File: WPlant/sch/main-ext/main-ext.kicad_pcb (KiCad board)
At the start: 2 copper layers, 156 parts, among them J1 PROG/JTAG, J10 Ext, J11 HSensor, J12 HSensor, J13 HSensor, J14 HSensor, J15 HSensor, J16 HSensor, J17 HSensor, J18 WaterLevel, J2 Battery, J3 Balance, J4 DE9_Receptacle, J6 Conn_01x08_Pin, J9 Leak, M1 Motor_DC, Q1 FDS9926A, Q2 FDS9926A, Q3 FDS9926A, Q4 FDS9926A, Q6 Si2301, Q7 BC817, SW1 SW_Push, SW2 SW_Push, SW3 SW_Push, U1 SIWG917Y121MGABAR, U10 SP485EEN-L/TR, U11 TXU0102QDCURQ1, U12 CD74HCT4051M96, U13 CD74HCT4051M96, U14 SN74LVC1G14DBV, U2 AP64352SP-13, U3 AP64352SP-13, U4 AP64352SP-13, U6 AP2204R-5.0, U7 74HC594, U9 INA180A2, X1 SIT1552AI-JE-DCC-32.768D

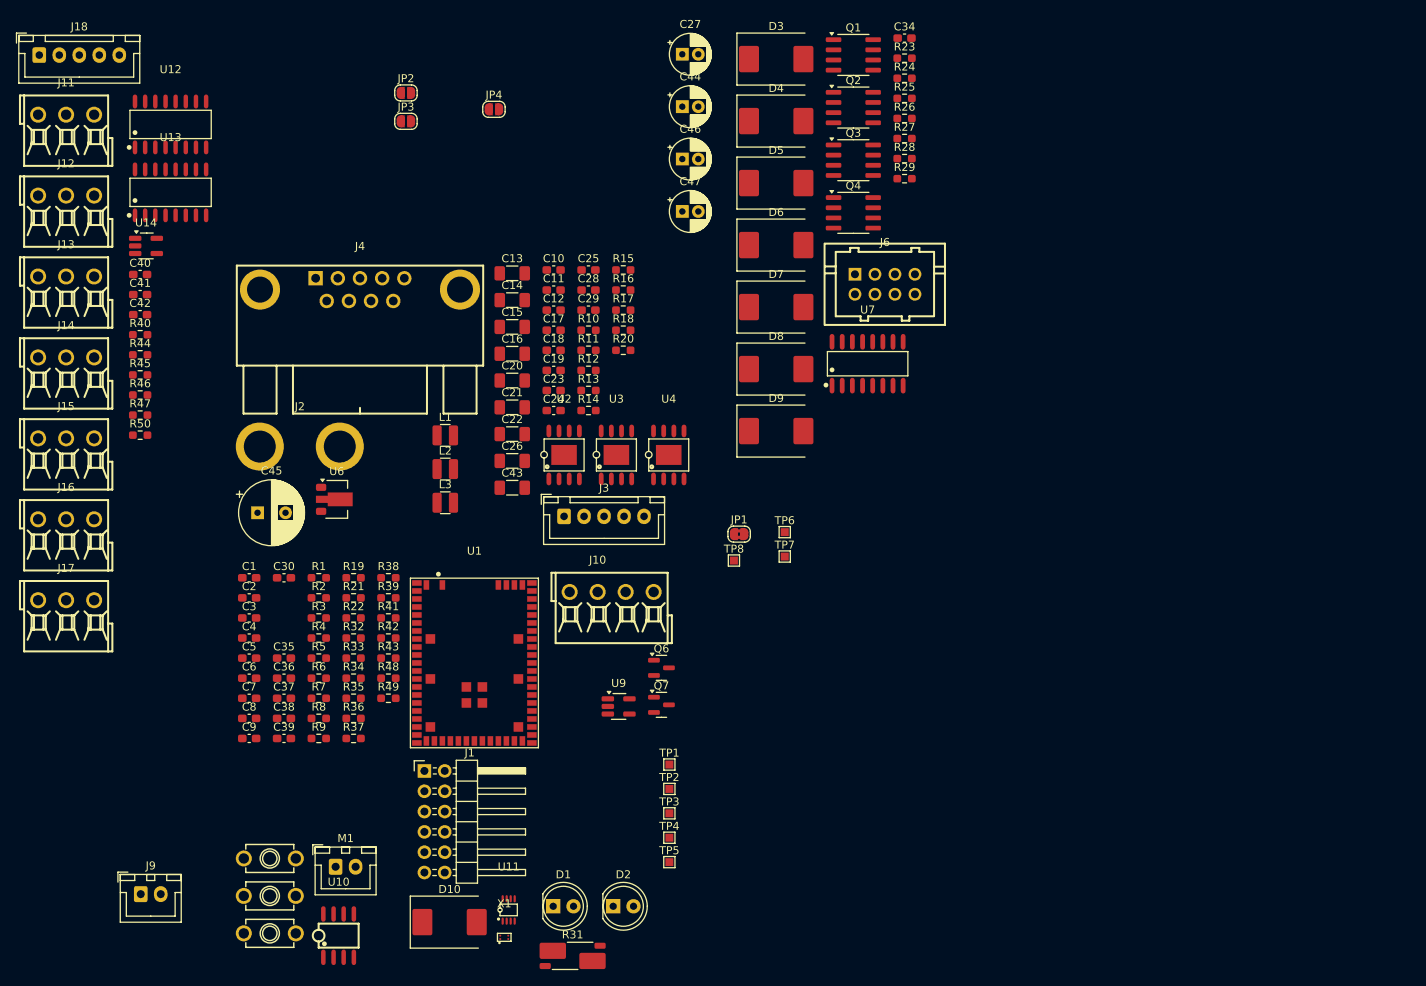
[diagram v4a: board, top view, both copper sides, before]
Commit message: Route of MainInt PCB done
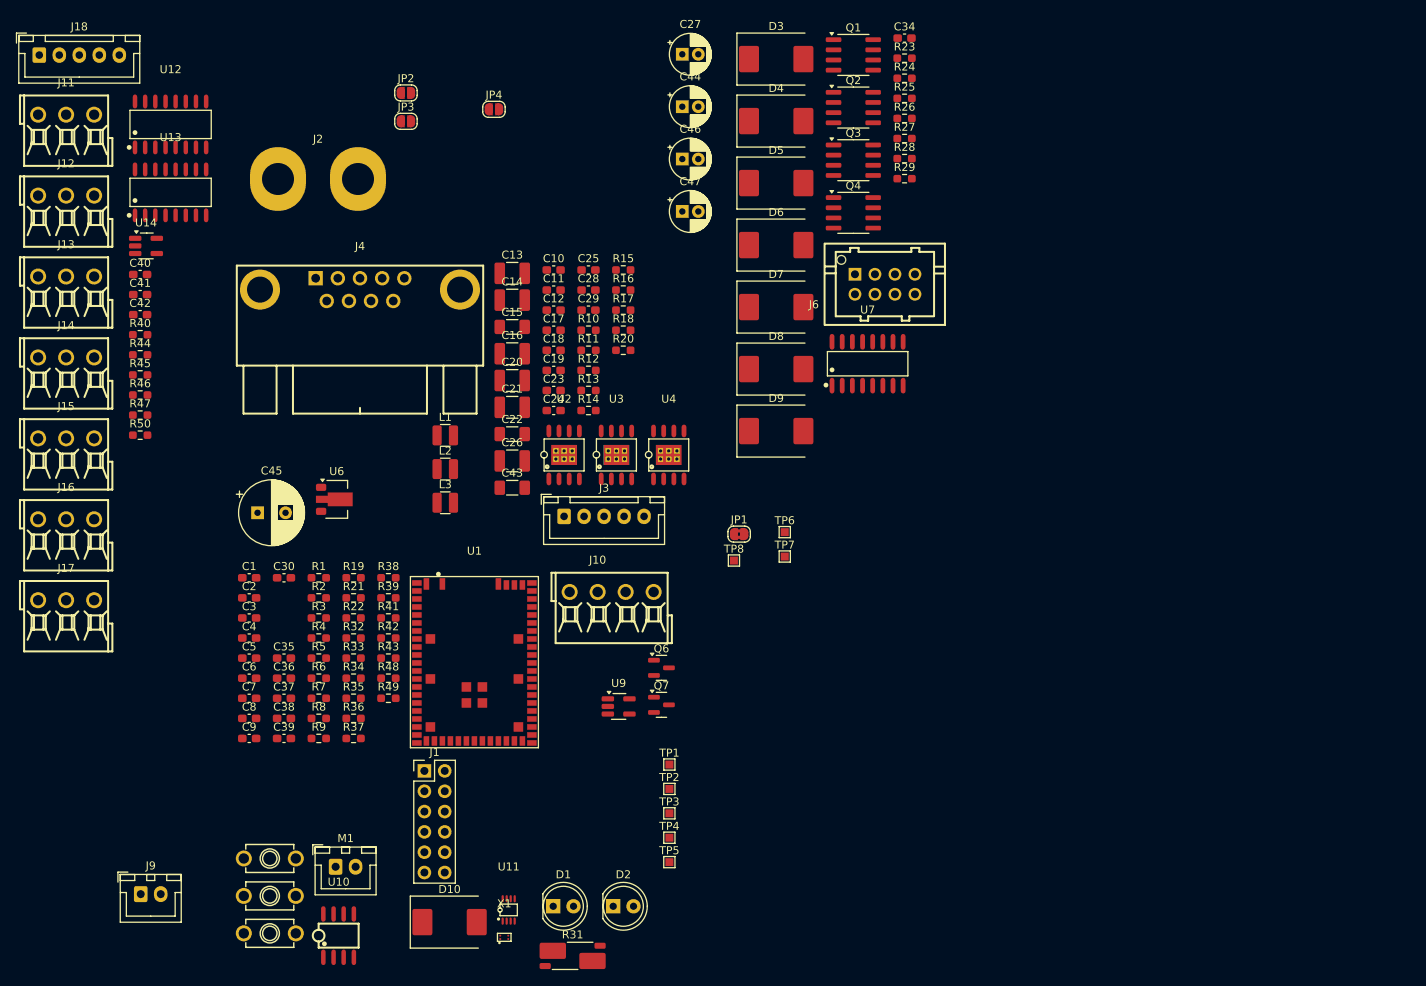
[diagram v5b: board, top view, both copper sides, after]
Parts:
- C13, C14, C16, C20, C21, C26: footprint Capacitor_SMD:C_1206_3216Metric_Pad1.33x1.80mm_HandSolder -> Capacitor_SMD:C_1210_3225Metric_Pad1.33x2.70mm_HandSolder
- J1: footprint locals:PinHeader_2x06_P2.54mm_HorizontalAB -> locals:PinHeader_2x06_P2.54mm_VerticalAB
- J6: footprint easyeda2kicad:CONN-TH_8P-P2.50_XAD-8A -> locals:CONN-TH_8P-P2.50_XAD-8AS
- U1: footprint easyeda2kicad:COMM-SMD_SIWG917Y110LGNBA -> locals:COMM-SMD_SIWG917Y110LGNBA
- U2, U3, U4: footprint easyeda2kicad:SO-8_L4.9-W3.9-P1.27-LS6.0-BL-EP -> locals:SO-8_L4.9-W3.9-P1.27-LS6.0-BL-EP
- moved J2 33.5 mm to (93.6, 57.2)

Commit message: Route of MainExt PCB done
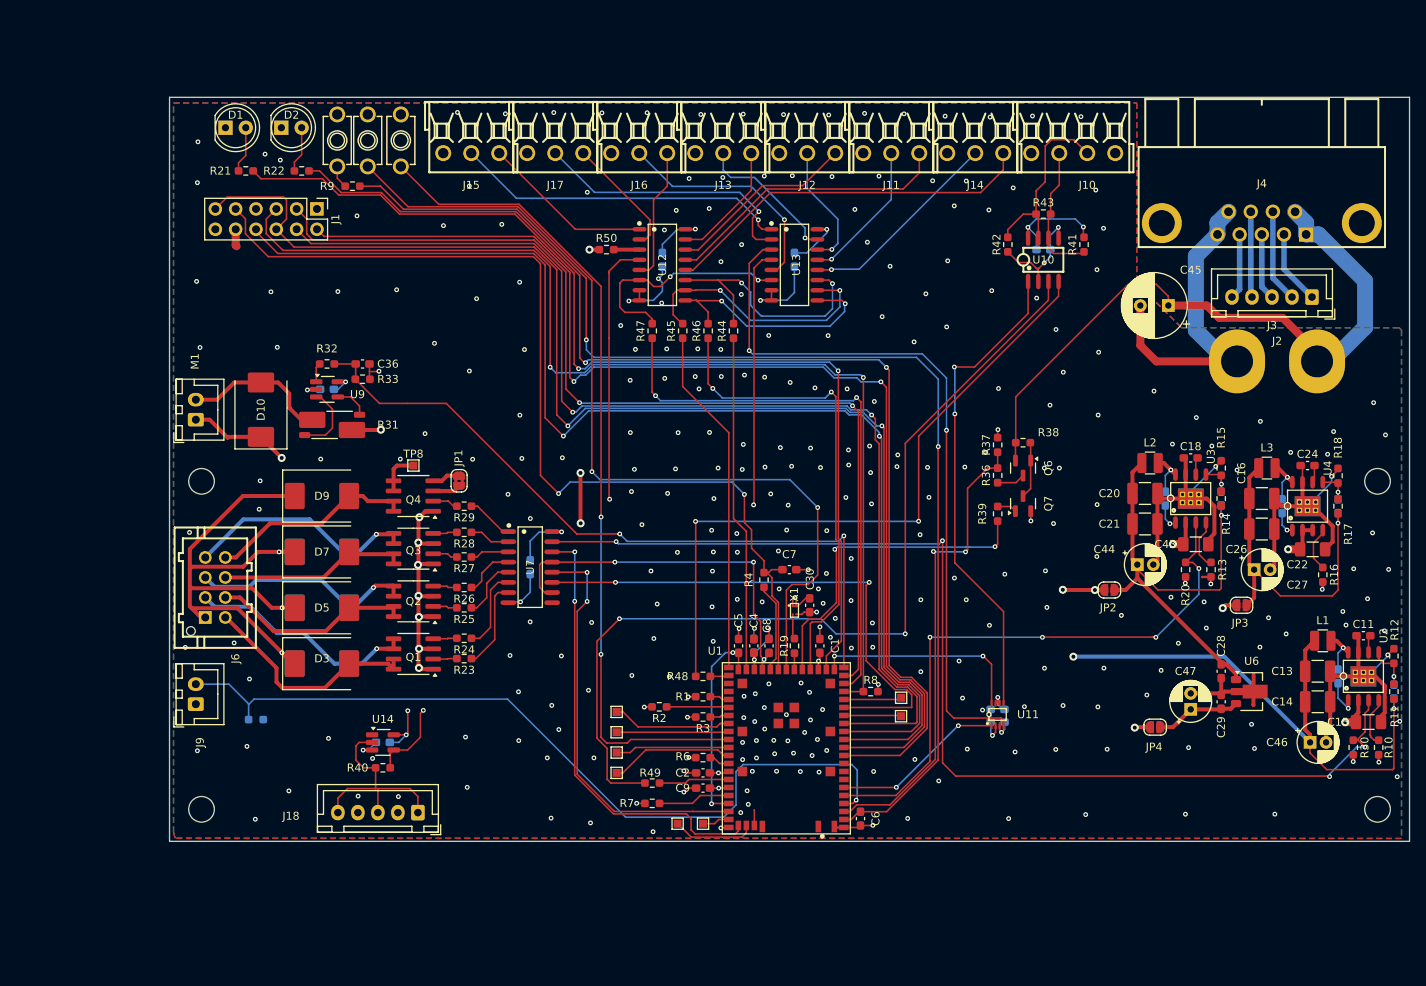
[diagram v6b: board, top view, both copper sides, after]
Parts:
- removed R34: 510, Resistor_SMD:R_0603_1608Metric_Pad0.98x0.95mm_HandSolder
- added H1: MountingHole, MountingHole:MountingHole_3.2mm_M3, F.Cu at (84.0, 95.0)
- added H2: MountingHole, MountingHole:MountingHole_3.2mm_M3, F.Cu at (231.0, 95.0)
- added H3: MountingHole, MountingHole:MountingHole_3.2mm_M3, F.Cu at (231.0, 136.0)
- added H4: MountingHole, MountingHole:MountingHole_3.2mm_M3, F.Cu at (84.0, 136.0)
- added R30: 200K, Resistor_SMD:R_0603_1608Metric_Pad0.98x0.95mm_HandSolder, F.Cu at (228.0, 128.3)
- added TP9: TestPoint, TestPoint:TestPoint_Pad_1.0x1.0mm, F.Cu at (146.7, 137.8)
- C10, C12, C17, C19, C23, C25, C3, C34, C35, C37, C38, C39, C40, C41, C42, D4, D6, D8, R35, R5: moved to B.Cu
- moved U10 122.1 mm to (189.2, 67.3)
- moved J2 122.0 mm to (213.4, 80.0)
- moved JP3 120.7 mm to (214.0, 110.5), turned to 180 degrees
- moved C15 117.9 mm to (229.9, 125.1), turned to 180 degrees
- moved U6 116.9 mm to (215.3, 121.3)
- moved C45 116.8 mm to (204.9, 73.0), turned to 180 degrees
- moved J14 116.5 mm to (180.7, 54.0), turned to 180 degrees
- moved C12 115.3 mm to (233.0, 121.3), turned to -90 degrees
- moved JP4 113.1 mm to (203.2, 125.7), turned to 180 degrees
- moved J4 113.0 mm to (216.5, 62.7), turned to 180 degrees
- moved L1 112.7 mm to (224.2, 114.9), turned to 180 degrees
- moved C14 112.5 mm to (223.5, 122.6), turned to 180 degrees
- moved C13 112.3 mm to (223.5, 118.7), turned to 180 degrees
- moved R10 111.7 mm to (231.1, 128.3), turned to -90 degrees
- moved C10 110.4 mm to (226.1, 119.4), turned to 90 degrees
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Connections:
- R23 pad 1: Net-(U7-QA) -> Net-(U7-QH)
- R24 pad 1: Net-(U7-QB) -> Net-(U7-QG)
- R25 pad 1: Net-(U7-QC) -> Net-(U7-QF)
- R26 pad 1: Net-(U7-QD) -> Net-(U7-QE)
- R27 pad 1: Net-(U7-QE) -> Net-(U7-QD)
- R28 pad 1: Net-(U7-QF) -> Net-(U7-QC)
- R29 pad 1: Net-(U7-QG) -> Net-(U7-QB)
- TP5 pad 1: Net-(U1-ULP_GPIO_1) -> Net-(U1-GPIO_15)
- U1 pad 28: Net-(U1-ULP_GPIO_1) -> /AccSence
- U1 pad 56: /Valves/MOSI -> Net-(U1-GPIO_12)
- U1 pad 58: Net-(U1-GPIO_11) -> /Valves/MOSI
- U1 pad 59: /AccSence -> Net-(U1-GPIO_15)
- U7 pad 15: Net-(U7-QA) -> /Power/EN12
- U7 pad 7: /Power/EN12 -> Net-(U7-QH)
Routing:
- net GND: track 0.00 -> 277.7 mm, vias 0 -> 325
- net +9V: track 0.00 -> 265.5 mm, vias 0 -> 5
- net +3.3V: track 0.00 -> 211.8 mm, vias 0 -> 16
- net +5V: track 0.00 -> 211.5 mm, vias 0 -> 8
- net /Power/12V: track 0.00 -> 209.2 mm, vias 0 -> 3
- net VBUS: track 0.00 -> 170.8 mm, vias 0 -> 3
- net JTAG-TDO: track 0.00 -> 163.0 mm, vias 0 -> 2
- net JTAG-TCK: track 0.00 -> 151.5 mm, vias 0 -> 2
- net Net-(U1-UULP_VBAT_GPIO_0): track 0.00 -> 150.0 mm, vias 0 -> 2
- net Net-(U1-GPIO_55): track 0.00 -> 148.5 mm, vias 0 -> 2
- net JTAG-TMS: track 0.00 -> 144.9 mm, vias 0 -> 2
- net JTAG-TDI: track 0.00 -> 142.4 mm, vias 0 -> 2
- net /Power/EN12: track 0.00 -> 139.9 mm, vias 0 -> 4
- net PROG-RX: track 0.00 -> 135.9 mm, vias 0 -> 2
- net Net-(U1-GPIO_52): track 0.00 -> 129.1 mm, vias 0 -> 2
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- added copper zone on In1.Cu, net +3.3V
- added copper zone on B.Cu, net GND
- added copper zone on F.Cu, net GND
- added copper zone on In1.Cu, net GND
- added copper zone on In2.Cu, net GND
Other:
- board outline added: 155 x 93 mm
- copper layers 2 -> 4

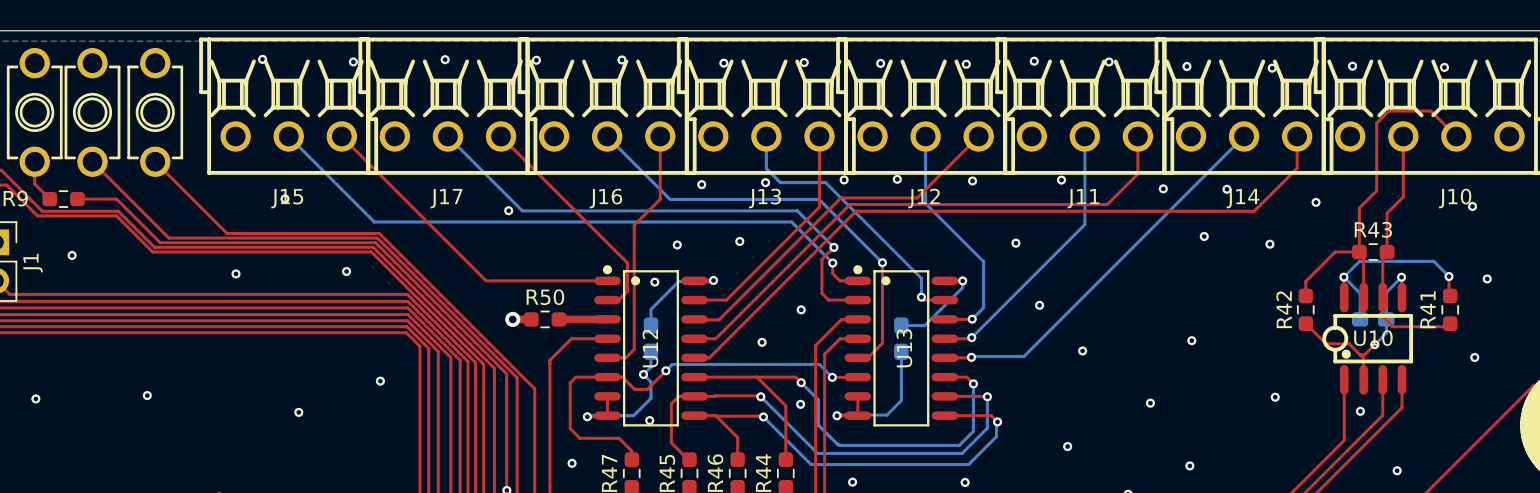
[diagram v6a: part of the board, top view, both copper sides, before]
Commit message: Route of WP project done
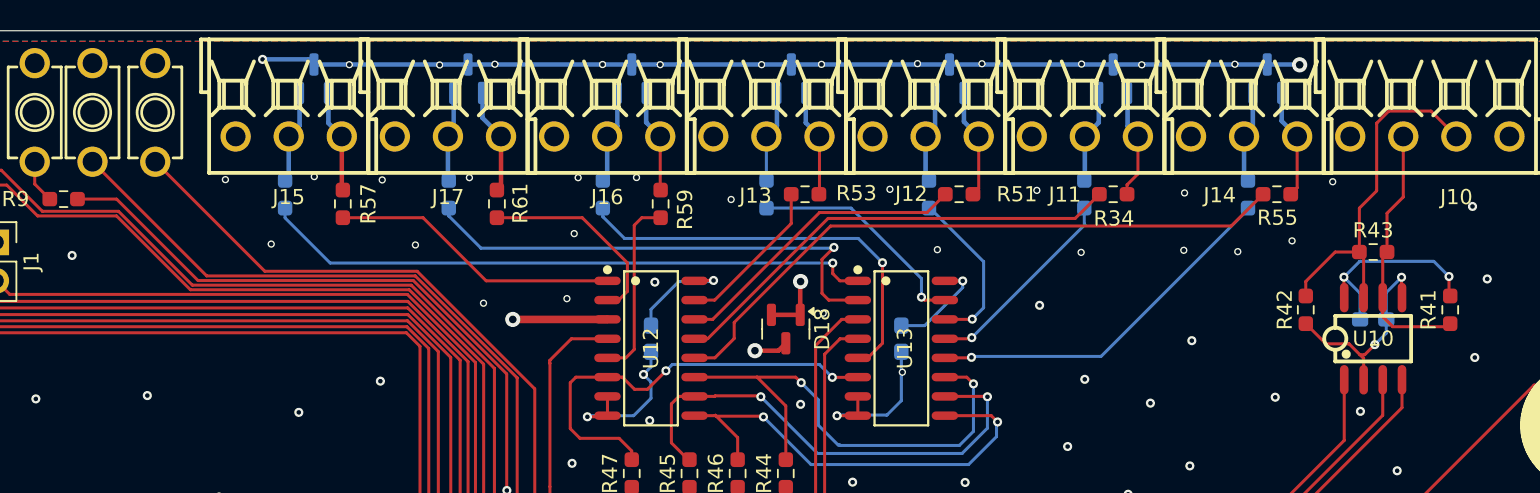
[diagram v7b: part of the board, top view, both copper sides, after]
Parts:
- added D11: MMBZ5V6, Package_TO_SOT_SMD:SOT-23, B.Cu at (172.1, 50.2)
- added D12: MMBZ5V6, Package_TO_SOT_SMD:SOT-23, B.Cu at (161.3, 50.2)
- added D13: MMBZ5V6, Package_TO_SOT_SMD:SOT-23, B.Cu at (150.9, 50.2)
- added D14: MMBZ5V6, Package_TO_SOT_SMD:SOT-23, B.Cu at (182.2, 50.2)
- added D15: MMBZ5V6, Package_TO_SOT_SMD:SOT-23, B.Cu at (119.4, 50.2)
- added D16: MMBZ5V6, Package_TO_SOT_SMD:SOT-23, B.Cu at (140.3, 50.2)
- added D17: MMBZ5V6, Package_TO_SOT_SMD:SOT-23, B.Cu at (129.5, 50.2)
- added D18: MMBZ5V6, Package_TO_SOT_SMD:SOT-23, F.Cu at (150.5, 66.7)
- added R34: 100, Resistor_SMD:R_0603_1608Metric_Pad0.98x0.95mm_HandSolder, F.Cu at (172.1, 57.8)
- added R51: 100, Resistor_SMD:R_0603_1608Metric_Pad0.98x0.95mm_HandSolder, F.Cu at (161.9, 57.8)
- added R52: 100, Resistor_SMD:R_0603_1608Metric_Pad0.98x0.95mm_HandSolder, B.Cu at (159.9, 57.8)
- added R53: 100, Resistor_SMD:R_0603_1608Metric_Pad0.98x0.95mm_HandSolder, F.Cu at (151.8, 57.8)
- added R54: 100, Resistor_SMD:R_0603_1608Metric_Pad0.98x0.95mm_HandSolder, B.Cu at (149.2, 57.8)
- added R55: 100, Resistor_SMD:R_0603_1608Metric_Pad0.98x0.95mm_HandSolder, F.Cu at (182.9, 57.8)
- added R56: 100, Resistor_SMD:R_0603_1608Metric_Pad0.98x0.95mm_HandSolder, B.Cu at (181.0, 57.8)
- added R57: 100, Resistor_SMD:R_0603_1608Metric_Pad0.98x0.95mm_HandSolder, F.Cu at (121.3, 58.4)
- added R58: 100, Resistor_SMD:R_0603_1608Metric_Pad0.98x0.95mm_HandSolder, B.Cu at (117.5, 57.8)
- added R59: 100, Resistor_SMD:R_0603_1608Metric_Pad0.98x0.95mm_HandSolder, F.Cu at (142.2, 58.4)
- added R60: 100, Resistor_SMD:R_0603_1608Metric_Pad0.98x0.95mm_HandSolder, B.Cu at (138.4, 57.8)
- added R61: 100, Resistor_SMD:R_0603_1608Metric_Pad0.98x0.95mm_HandSolder, F.Cu at (131.4, 58.4)
- added R62: 100, Resistor_SMD:R_0603_1608Metric_Pad0.98x0.95mm_HandSolder, B.Cu at (128.3, 57.8)
- R50: moved to B.Cu
- moved R50 36.5 mm to (170.2, 57.8), turned to 90 degrees
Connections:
- J11 pad 1: /Humidity/P1 -> Net-(J11-Pin_1)
- J11 pad 2: /Humidity/F1 -> Net-(J11-Pin_2)
- J12 pad 1: /Humidity/P2 -> Net-(J12-Pin_1)
- J12 pad 2: /Humidity/F2 -> Net-(J12-Pin_2)
- J13 pad 1: /Humidity/P3 -> Net-(J13-Pin_1)
- J13 pad 2: /Humidity/F3 -> Net-(J13-Pin_2)
- J14 pad 1: /Humidity/P4 -> Net-(J14-Pin_1)
- J14 pad 2: /Humidity/F4 -> Net-(J14-Pin_2)
- J15 pad 1: /Humidity/P5 -> Net-(J15-Pin_1)
- J15 pad 2: /Humidity/F5 -> Net-(J15-Pin_2)
- J16 pad 1: /Humidity/P6 -> Net-(J16-Pin_1)
- J16 pad 2: /Humidity/F6 -> Net-(J16-Pin_2)
- J17 pad 1: /Humidity/P7 -> Net-(J17-Pin_1)
- J17 pad 2: /Humidity/F7 -> Net-(J17-Pin_2)
- R50 pad 1: +5V -> /Humidity/F1
- R50 pad 2: Net-(U12-A) -> Net-(J11-Pin_2)
- U12 pad 3: Net-(U12-A) -> +5V
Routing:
- net GND: track 277.7 -> 348.7 mm, vias 325 -> 328
- net +5V: track 211.5 -> 220.6 mm, vias 8 -> 9
- net Net-(J12-Pin_1): track 0.00 -> 7.72 mm
- net Net-(J14-Pin_1): track 0.00 -> 7.28 mm
- net Net-(J11-Pin_1): track 0.00 -> 7.26 mm
- net Net-(J13-Pin_1): track 0.00 -> 7.07 mm
- net Net-(J17-Pin_1): track 0.00 -> 7.02 mm
- net Net-(J16-Pin_1): track 0.00 -> 6.80 mm
- net Net-(J15-Pin_1): track 0.00 -> 6.80 mm
- net Net-(J15-Pin_2): track 0.00 -> 6.17 mm
- net Net-(J16-Pin_2): track 0.00 -> 6.17 mm
- net Net-(J11-Pin_2): track 0.00 -> 6.17 mm
- net Net-(J12-Pin_2): track 0.00 -> 6.12 mm
- net Net-(J14-Pin_2): track 0.00 -> 6.12 mm
- net Net-(J13-Pin_2): track 0.00 -> 6.06 mm
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
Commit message: Added connectors marks on back of PCBs
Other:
- board text added: "+"
- board text added: "-"
- board text added: "1"
- board text added: "2"
- board text added: "3"
- board text added: "4"
- board text added: "5"
- board text added: "6"
- board text added: "7"
- board text added: "A"
- board text added: "B"
